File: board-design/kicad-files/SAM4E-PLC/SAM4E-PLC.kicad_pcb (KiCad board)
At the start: 2 copper layers, 86.1 x 174.1 mm, 280 parts, among them J1 Conn_ARM_JTAG_SWD_10, J2 0473460001, J3 Conn_02x05_Odd_Even, J4 Conn_02x10_Odd_Even, J5 Screw_Terminal_01x11, J6 Screw_Terminal_01x11, J7 Screw_Terminal_01x11, J8 Screw_Terminal_01x11, Q1 BC807, Q10 BC807, Q11 BC817, Q2 BC807, Q3 BC807, Q4 BC807, Q5 BC807, Q6 BC807, Q7 BC807, Q8 BC807, Q9 BC807, U1 LM385M-ADJ, U10 SN74HC240DBR, U11 LM2576HVS-3.3, U2 ATSAM4E16E, U3 SN65HVD234, U4 SN65HVD234, U5 MAX31865xAP, U6 MAX3485ESA+T, U7 MAX31865xAP, U8 ULN2803CDWR, U9 74AC14SCX, Y1 ECS-160-8-33B-CTN-TR, Y2 FC-135 32.7680KA-AG0

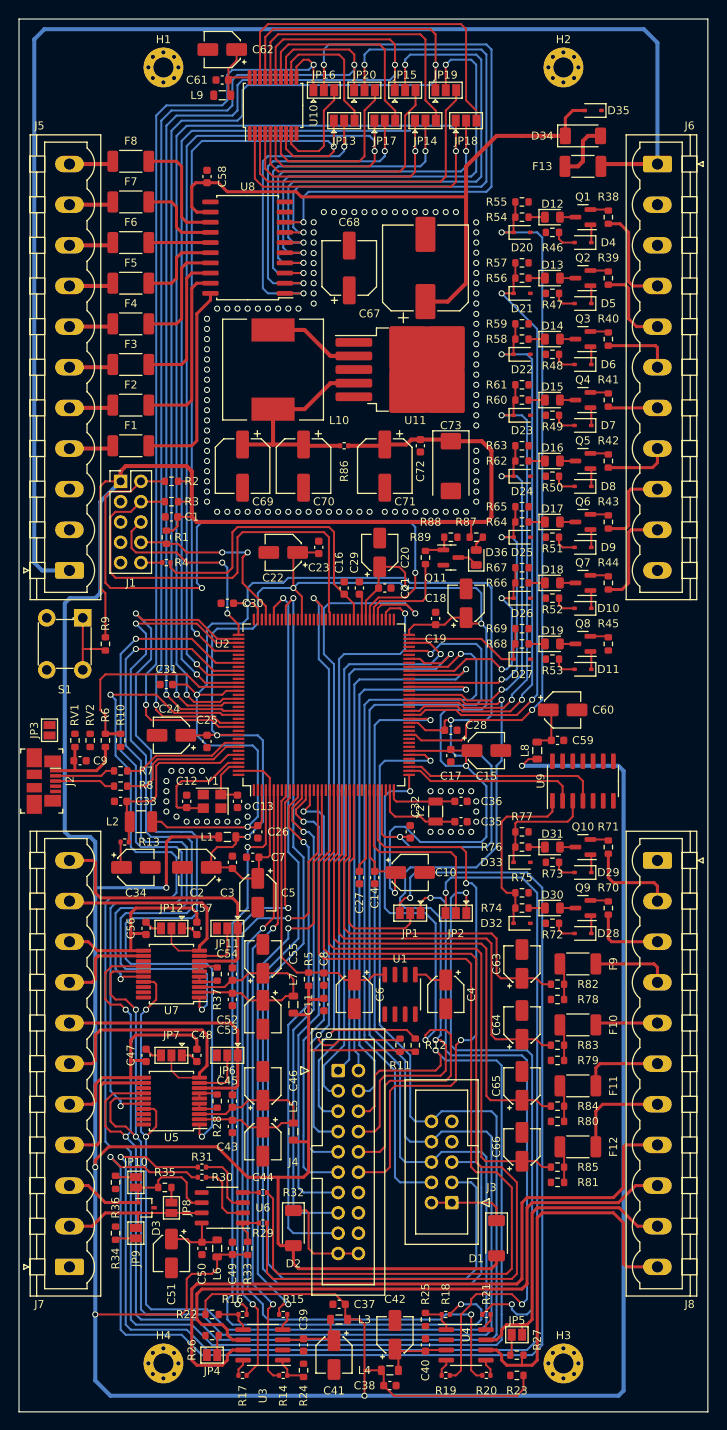
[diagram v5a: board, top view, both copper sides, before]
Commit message: [UPDATE]
Completed SAM4E-PLC board design.

Signed-off-by: Nicolae-Andrei Vasile <vasilenicolaeandrei@gmail.com>
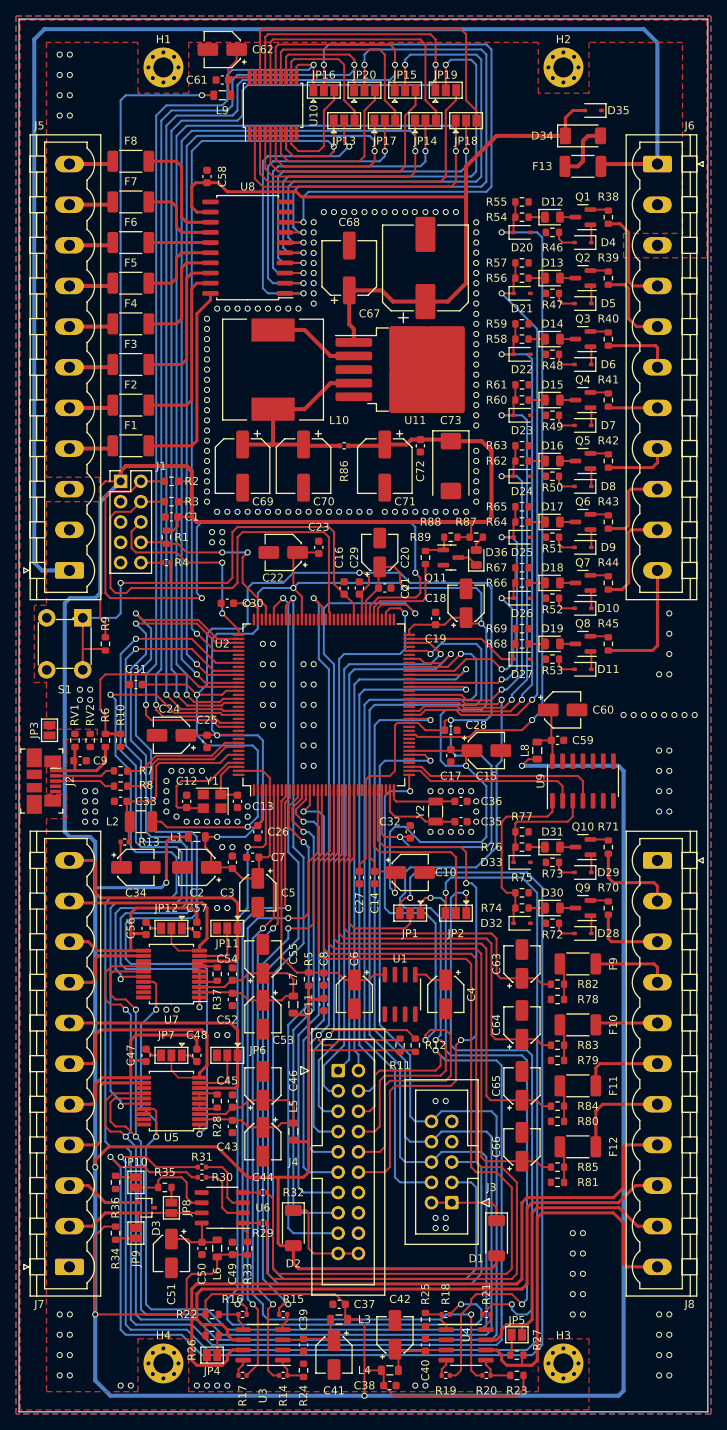
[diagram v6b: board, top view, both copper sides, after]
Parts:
- R26, R27: value 120R/R0402 -> 120R/R0603
- moved L1 3.81 mm to (98.4, 121.3)
- moved C31 3.81 mm to (90.8, 102.2)
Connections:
- H1 pad 1: Earth_Protective -> (no net)
- H2 pad 1: Earth_Protective -> (no net)
- H3 pad 1: Earth_Protective -> (no net)
- H4 pad 1: Earth_Protective -> (no net)
- J2 pad SH: Net-(J2-PadSH) -> Earth_Protective
- RV1 pad 2: Net-(J2-PadSH) -> Earth_Protective
- RV2 pad 2: Net-(J2-PadSH) -> Earth_Protective
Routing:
- net +3V3: track 610.4 -> 680.2 mm, vias 5 -> 6
- net Net-(U2-VDDOUT): track 187.7 -> 209.1 mm, vias 5 -> 6
- net /~{NRST}: track 47.9 -> 65.9 mm, vias 0 -> 1
- net +24V: track 80.0 -> 96.9 mm
- net /IO/MCV_DI7: track 0.00 -> 15.8 mm
- net Net-(J1-SWDIO/TMS): track 83.0 -> 86.8 mm
- net Net-(J1-SWCLK/TCK): track 57.7 -> 61.1 mm
- net Net-(U9-VCC): track 5.76 -> 8.43 mm
- net Net-(U4-EN): track 2.14 -> 4.62 mm
- net /~{RTD1_DRDY}: track 89.3 -> 87.5 mm
- net MCV_CAN1_L: track 79.2 -> 80.7 mm
- net /IO/DO1: track 133.7 -> 135.2 mm
- net /~{RTD0_DRDY}: track 107.3 -> 105.7 mm
- net MCV_CAN1_H: track 91.0 -> 92.2 mm
- net Net-(U2-VDDIN): track 231.5 -> 232.7 mm
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- added copper zone on F.Cu, net Earth_Protective
- added copper zone on B.Cu, net GND
- added copper zone on F.Cu, net GND
